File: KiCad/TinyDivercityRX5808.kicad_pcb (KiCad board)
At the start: 2 copper layers, 22 x 20 mm, 23 parts, among them J1 Googles, J2 RX_A, J3 RX_B, J4 Conn_01x06, SW1 SW_Push, U1 MAX4624, U2 ATTINY85-20MU

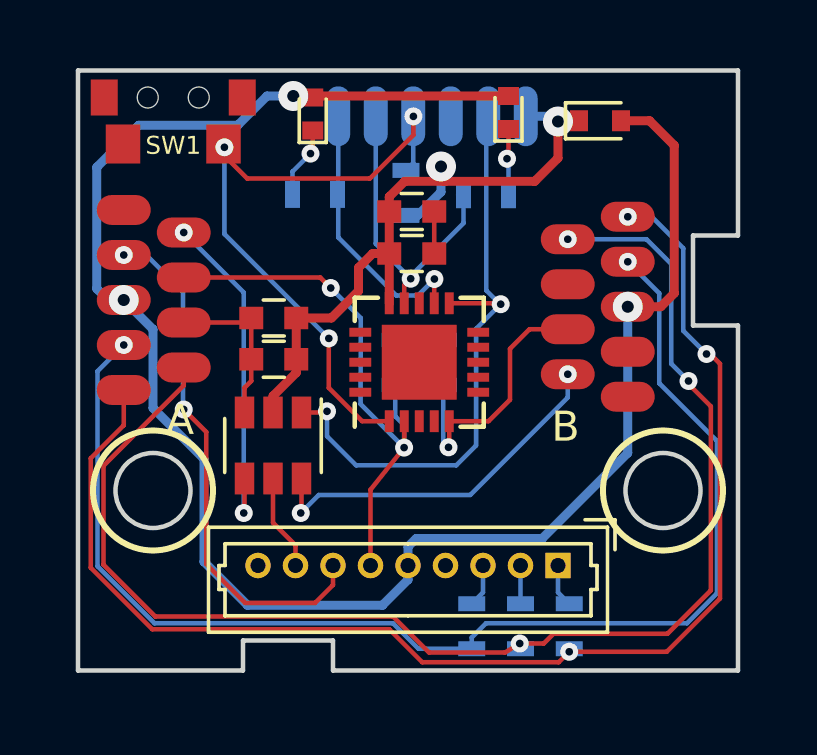
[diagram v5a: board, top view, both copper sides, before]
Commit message: Changed attiny case from QFN to SOIC8
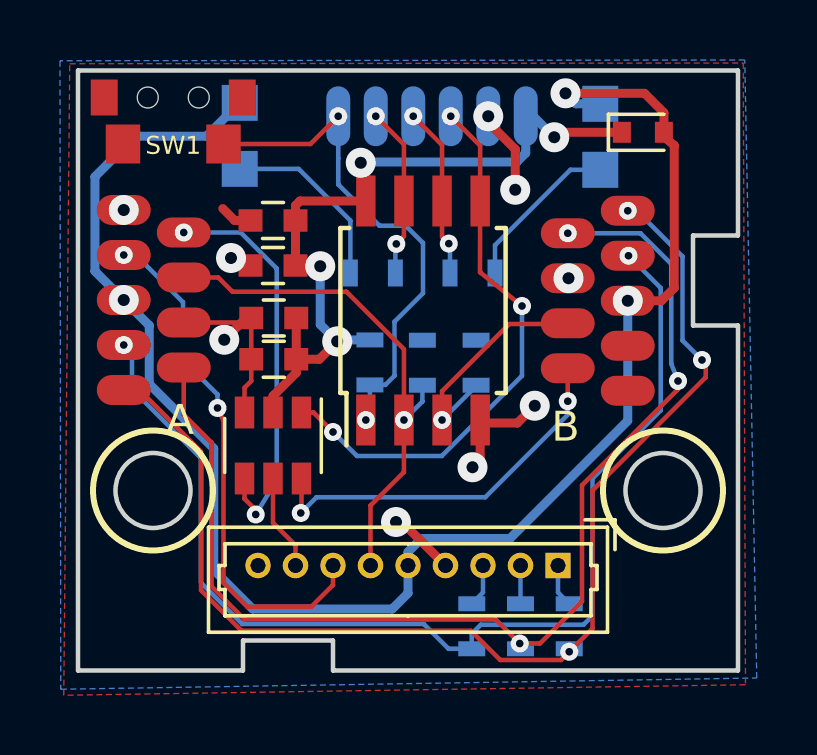
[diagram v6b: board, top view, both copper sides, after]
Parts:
- D1, D2: footprint LEDs:LED_0402 -> LEDs:LED_0805; moved to B.Cu
- U2: value ATTINY85-20MU -> ATTINY85-20SU; footprint Housings_DFN_QFN:QFN-20-1EP_4x4mm_Pitch0.5mm -> Housings_SOIC:SOIJ-8_5.3x5.3mm_Pitch1.27mm
- moved D2 9.62 mm to (146.2, 94.3)
- moved D1 8.99 mm to (134.2, 94.2)
- moved R7 5.87 mm to (141.9, 98.8), turned to 0 degrees
- moved R9 5.78 mm to (138.5, 101.8), turned to 90 degrees
- moved C4 4.64 mm to (135.3, 98.5), turned to 0 degrees
- moved C3 4.63 mm to (135.3, 97.0), turned to 0 degrees
- moved R6 4.59 mm to (138.6, 98.8), turned to 180 degrees
- moved U2 1.73 mm to (140.3, 100.0)
- moved D3 1.48 mm to (147.6, 94.1)
- moved R5 1.10 mm to (142.1, 101.8)
- moved R4 0.91 mm to (140.3, 101.8)
- moved J3 0.20 mm to (147.1, 99.7)
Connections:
- J4 pad 2: /MOSI -> GND
- J4 pad 3: GND -> /MOSI
- J4 pad 4: /RST -> /MISO
- J4 pad 6: /MISO -> /RST
- U2 pad 3: (no net) -> /RSSI_B
- U2 pad 4: (no net) -> GND
- U2 pad 5: /RSSI_B -> /MOSI
- U2 pad 6: (no net) -> /MISO
- U2 pad 7: (no net) -> /SCK
- U2 pad 8: GND -> /PROG_PWR
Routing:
- net GND: track 6.99 -> 18.3 mm, vias 0 -> 9
- net Net-(J2-Pad2): track 45.4 -> 38.3 mm
- net VCC: track 60.8 -> 54.9 mm
- net Net-(J2-Pad3): track 42.8 -> 37.1 mm
- net Net-(J2-Pad1): track 44.2 -> 39.3 mm
- net /SCK: track 10.5 -> 5.73 mm, vias 1 -> 2
- net /MISO: track 9.89 -> 5.73 mm, vias 1 -> 2
- net Net-(D1-Pad1): track 2.23 -> 6.15 mm, vias 1 -> 0
- net /RST: track 22.2 -> 18.3 mm, vias 3 -> 2
- net Net-(D2-Pad1): track 2.41 -> 5.48 mm, vias 1 -> 0
- net /PROG_PWR: track 23.8 -> 26.0 mm, vias 2 -> 4
- net /VideoA: track 11.3 -> 13.4 mm
- net /MOSI: track 20.6 -> 18.8 mm, vias 2 -> 3
- net /RSSI_B: track 9.25 -> 7.73 mm
- net /RSSI_A: track 18.8 -> 17.4 mm, vias 2 -> 1
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- added copper zone on B.Cu, net GND
- added copper zone on F.Cu, net GND

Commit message: Ready for production version
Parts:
- added D1: LED, LEDs:LED_0805, F.Cu at (132.6, 92.8)
- added D2: LED, LEDs:LED_0805, F.Cu at (147.0, 92.8)
- added REF**: MountingHole_2.5mm, Mounting_Holes:MountingHole_2.5mm, F.Cu at (148.3, 106.0)
- added REF**: MountingHole_2.5mm, Mounting_Holes:MountingHole_2.5mm, F.Cu at (131.3, 106.0)
- added REF**: SolderWirePad_single_0-8mmDrill, Connectors:Pin_d0.7mm_L6.5mm_W1.8mm_FlatFork, F.Cu at (131.5, 91.8)
- added REF**: SolderWirePad_single_0-8mmDrill, Connectors:Pin_d0.7mm_L6.5mm_W1.8mm_FlatFork, F.Cu at (133.7, 92.0)
- added REF**: SolderWirePad_single_0-8mmDrill, Connectors:Pin_d0.7mm_L6.5mm_W1.8mm_FlatFork, F.Cu at (145.9, 92.0)
- added REF**: SolderWirePad_single_0-8mmDrill, Connectors:Pin_d0.7mm_L6.5mm_W1.8mm_FlatFork, F.Cu at (148.1, 92.0)
- J4: moved to F.Cu
- SW1: moved to B.Cu
- moved SW1 7.80 mm to (139.8, 92.8), turned to 180 degrees
- moved D1 2.14 mm to (132.6, 92.8), turned to 180 degrees
- moved D2 1.63 mm to (147.0, 92.8), turned to 0 degrees
- moved D3 1.25 mm to (148.7, 94.8)
- moved R8 0.81 mm to (132.3, 100.6)
- moved J4 0.61 mm to (140.4, 94.2)
- moved C4 0.34 mm to (135.6, 98.5)
- moved C3 0.32 mm to (135.6, 97.1)
- moved C2 0.29 mm to (135.6, 100.3)
- moved C1 0.29 mm to (135.6, 101.7)
- moved U2 0.13 mm to (140.3, 100.2)
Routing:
- net GND: track 18.3 -> 31.7 mm, vias 9 -> 13
- net /RST: track 18.3 -> 11.9 mm
- net Net-(D1-Pad1): track 6.15 -> 9.88 mm, vias 0 -> 1
- net Net-(D2-Pad1): track 5.48 -> 8.79 mm, vias 0 -> 1
- net Net-(J2-Pad3): track 37.1 -> 38.3 mm
- net /PROG_PWR: track 26.0 -> 24.9 mm
- net VCC: track 54.9 -> 56.1 mm, vias 3 -> 4
- net /MOSI: track 18.8 -> 17.9 mm, vias 3 -> 2
- net /AUD_IN: track 12.7 -> 13.5 mm
- net /AUD_OUT: track 3.53 -> 2.87 mm
- net /MISO: track 5.73 -> 5.19 mm, vias 2 -> 1
- net /SCK: track 5.73 -> 5.19 mm, vias 2 -> 1
- net Net-(J2-Pad2): track 38.3 -> 38.6 mm, vias 3 -> 4
- net /RSSI_B: track 7.73 -> 7.87 mm, vias 1 -> 2
- net /RSSI_A: vias 1 -> 2
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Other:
- outline, holes or cut-outs redrawn
- net class Default: trace_width 0.1524 -> 0.2
- board text added: "+"
- board text added: "1"
- board text added: "2"
- board text added: "3"
- board text added: "5V"
- board text added: "G"
- board text added: "GND"
- board text added: "R"
- board text added: "RST"
- board text added: "V"
- board text removed: "PROG"

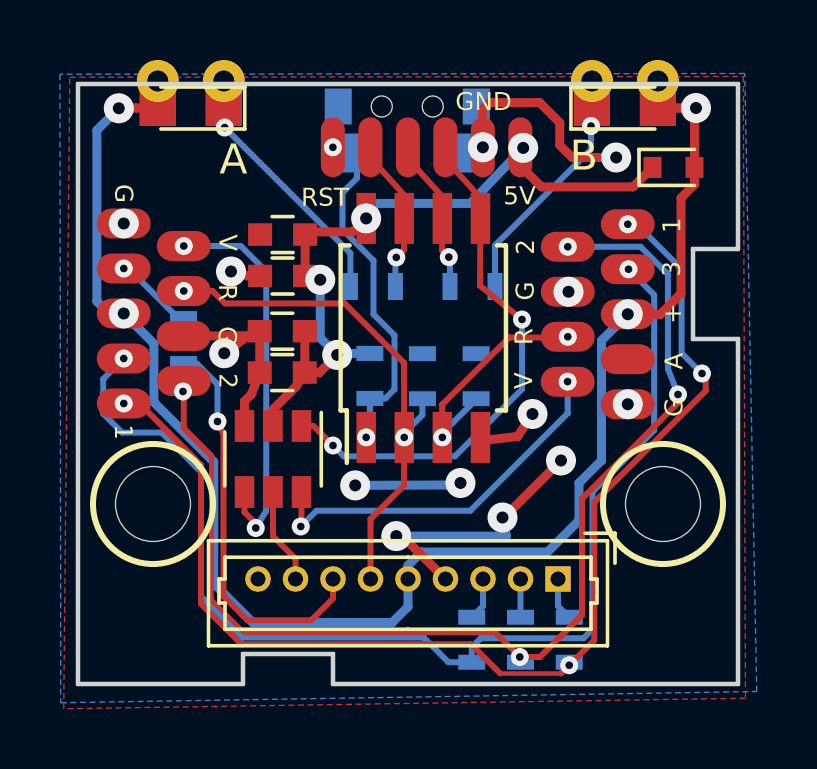
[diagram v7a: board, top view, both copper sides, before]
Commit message: Adjusted holes distance
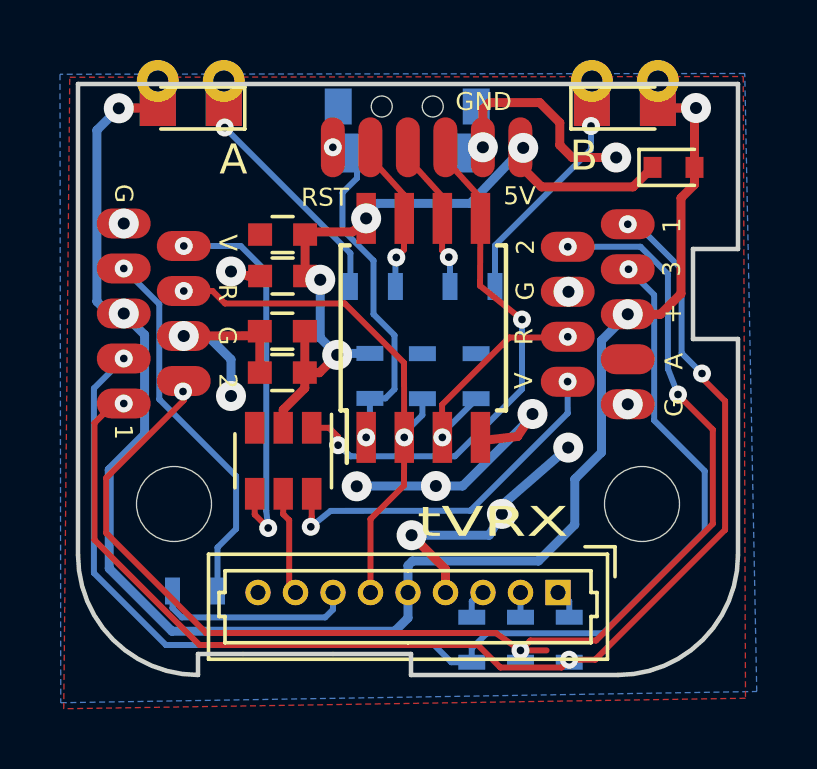
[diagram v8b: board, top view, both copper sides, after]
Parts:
- moved R8 8.34 mm to (132.7, 109.0), turned to 0 degrees
- moved REF** 0.70 mm to (132.0, 106.0)
- moved J1 0.45 mm to (144.8, 109.0)
- moved U1 0.35 mm to (135.6, 104.6)
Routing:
- net /AUD_OUT: track 2.87 -> 12.6 mm
- net /AUD_IN: track 13.5 -> 6.73 mm, vias 1 -> 0
- net Net-(J2-Pad2): track 38.6 -> 44.1 mm
- net VCC: track 56.1 -> 59.3 mm
- net Net-(J2-Pad3): track 38.3 -> 41.0 mm
- net GND: track 31.7 -> 34.4 mm, vias 13 -> 14
- net Net-(J2-Pad1): track 39.3 -> 41.8 mm
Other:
- board size 22 x 20 mm -> 22 x 19.7 mm
- board text added: "100K"
- board text added: "10K"
- board text added: "1K"
- board text added: "1Kx3"
- board text added: "30"
- board text added: "tVRX"
